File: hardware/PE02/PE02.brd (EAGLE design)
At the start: 25.4 x 25.4 mm, 24 parts, among them IC1 MSP430G2231, IC2 TPS78233

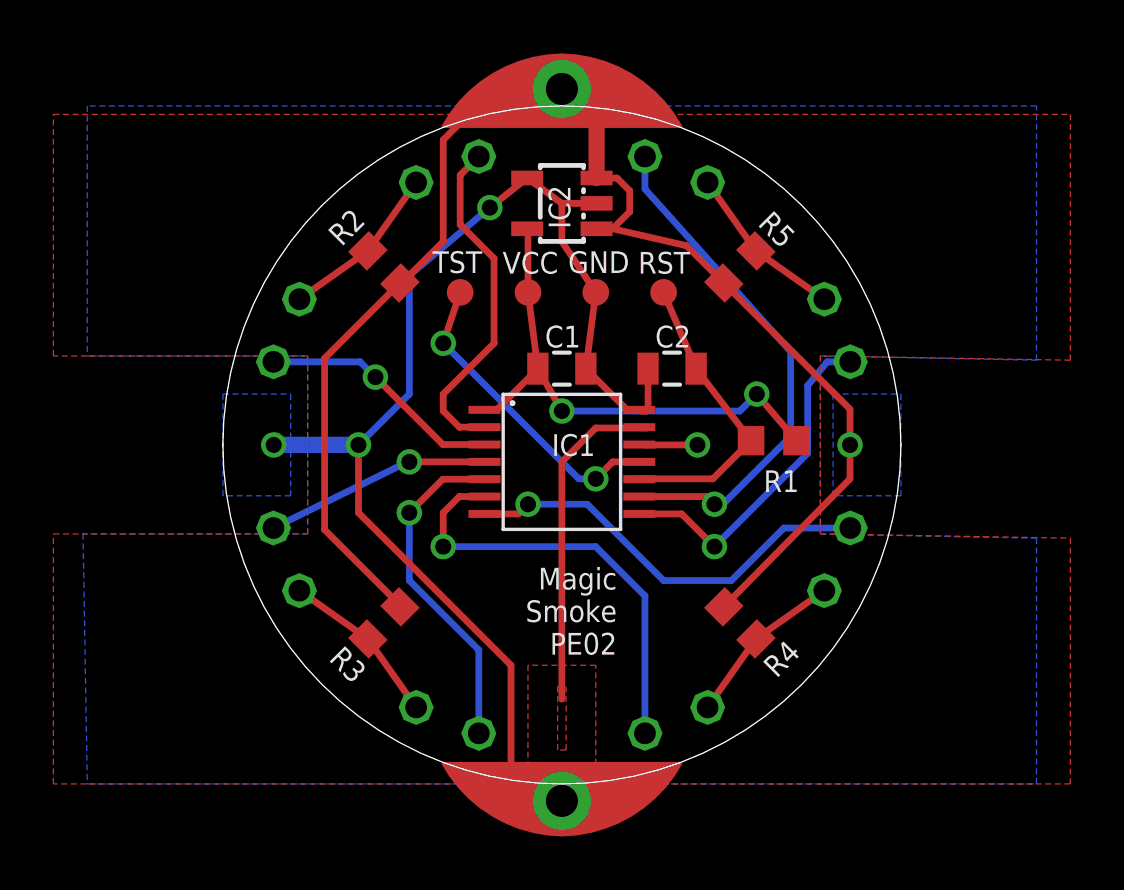
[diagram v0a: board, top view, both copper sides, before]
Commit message: Fixed buzzer, need to alter package of GND sewtab to make pad for vibration sensor
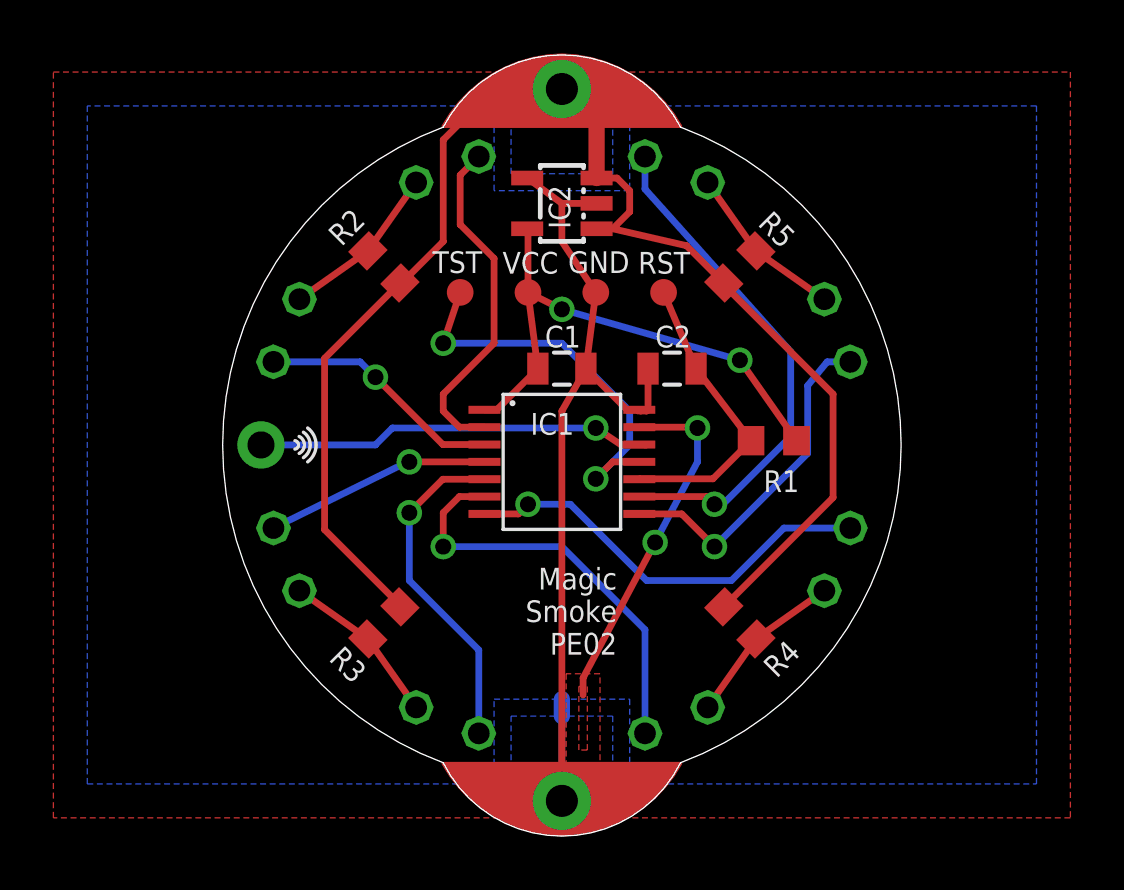
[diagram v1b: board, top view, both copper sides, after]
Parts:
- added JP1: (no value), adafruit:1X01-CLEANBIG
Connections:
- net BUZZ: now also JP1.1
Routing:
- net BUZZ: track 2.18 -> 15.2 mm
- net GND: track 47.0 -> 34.4 mm, vias 3 -> 0
- net TST: track 11.7 -> 15.0 mm
- net N$2: track 16.5 -> 15.8 mm
- net V+: track 54.2 -> 53.7 mm, vias 1 -> 0
- net VIB: track 12.9 -> 13.3 mm, vias 0 -> 2
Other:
- board size 25.4 x 25.4 mm -> 25.4 x 29.3 mm

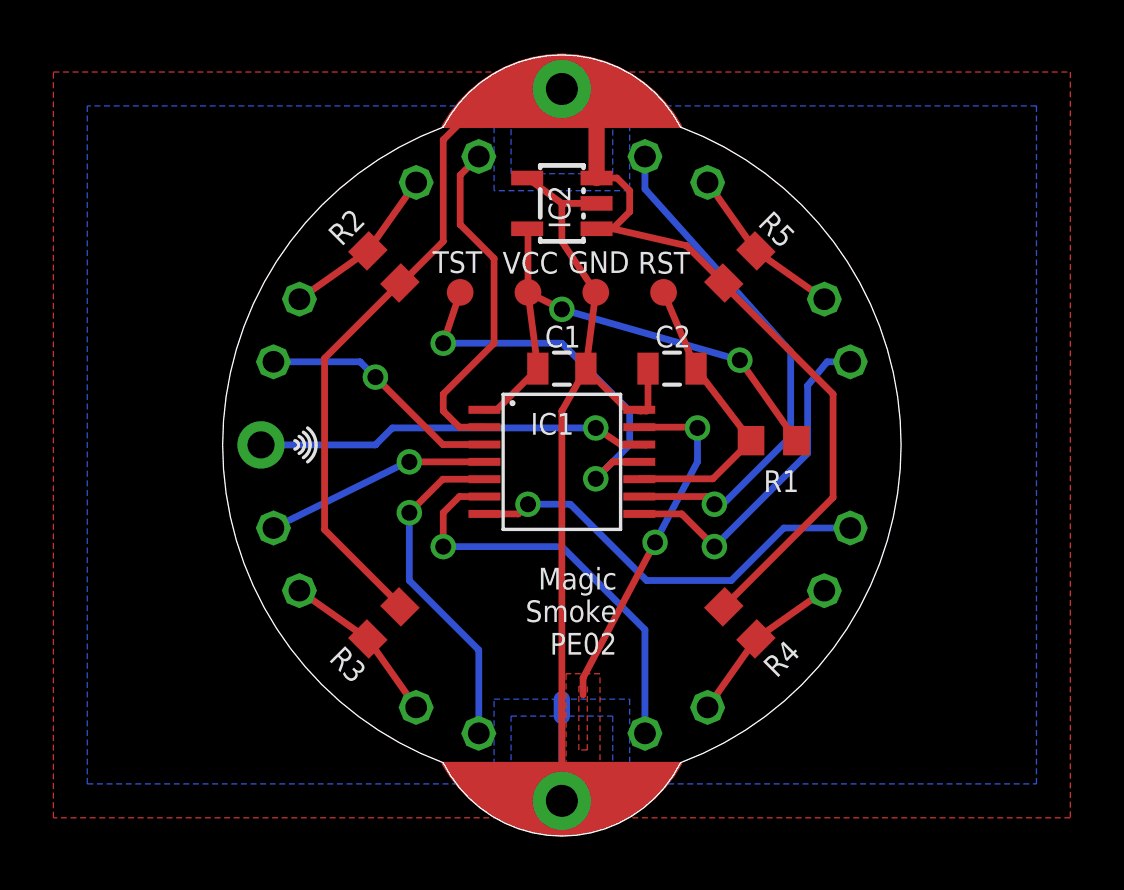
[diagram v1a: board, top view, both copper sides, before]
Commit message: 2.2V supply, pullup vibration sensor to output pin
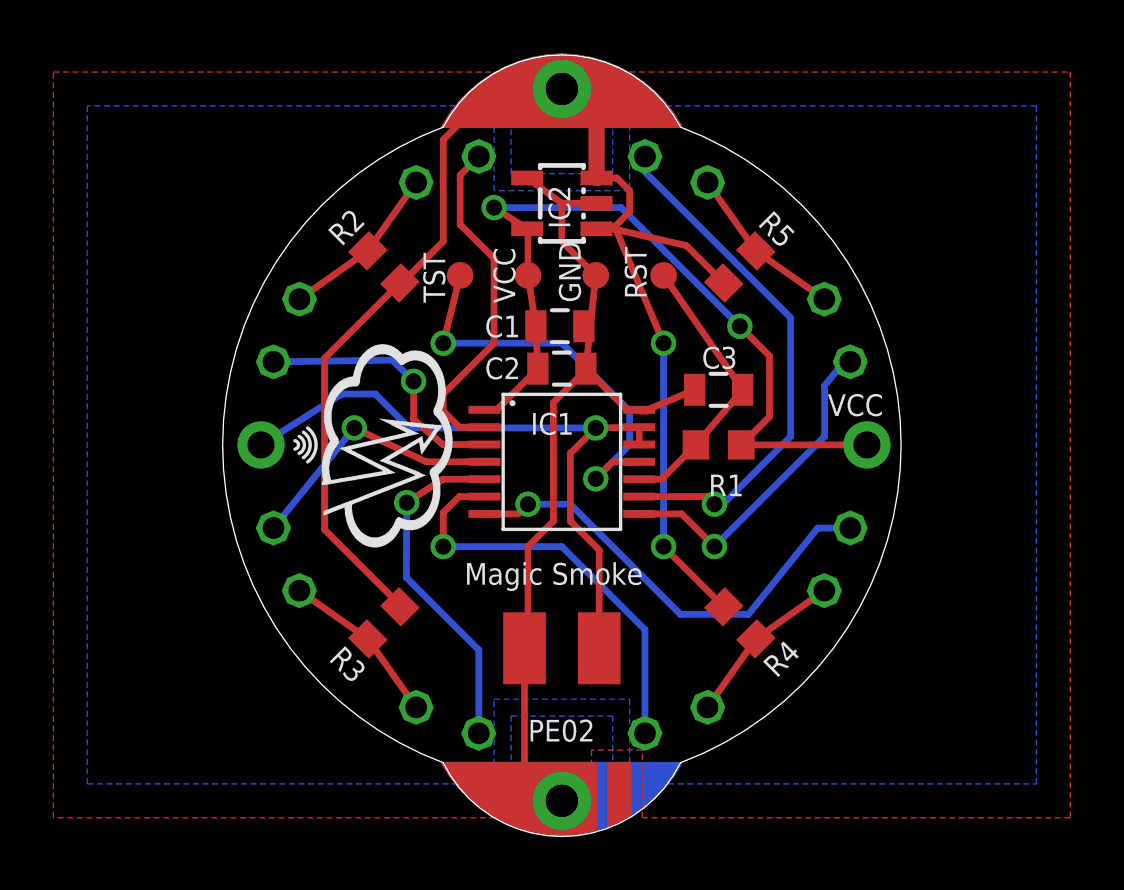
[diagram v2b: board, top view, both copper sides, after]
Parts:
- added C3: 1nF, SparkFun:0805
- added JP2: (no value), adafruit:1X01-CLEANBIG
- added MVS0608.02: (no value), rcl:R1210
- added TP3: SEWTAP0.4IN, adafruit:SEWINGTAP_0.4
- added TP4: SEWTAB, t0mpr1c3:SEWTAP_CUSTOM
- C1: value 100nF -> 1uF
- C2: value 1nF -> 100nF
- IC2: value TPS78233 -> TPS78222
- moved TP2 26.7 mm to (50.8, 69.2), flipped to the bottom, turned to 0 degrees
- moved C2 4.13 mm to (50.8, 58.7), turned to 0 degrees
- moved R1 2.07 mm to (56.7, 55.9)
- moved C1 1.59 mm to (50.7, 60.3)
- moved GND 0.63 mm to (52.1, 62.2)
- moved RST 0.63 mm to (54.6, 62.2)
- moved TST 0.63 mm to (47.0, 62.2)
- moved VCC 0.63 mm to (49.5, 62.2)
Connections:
- removed net +3V3: C1.1, IC1.1, IC2.5, R1.2, VCC.TP
- removed net BUZZ: IC1.12, JP1.1
- new net VCC: C1.1, C2.1, IC1.1, IC2.5, JP2.1, R1.2, VCC.TP
- net GND: now also C3.2, MVS0608.02.1, TP3.TAP, TP4.TAP; no longer TP2.TAP
- net RST: now also C3.1; no longer C2.1
- net V+: now also TP2.TAP
- net VIB: now also IC1.12, JP1.1, MVS0608.02.2
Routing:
- net VCC: track 0.00 -> 30.5 mm, vias 0 -> 2
- net +3V3: track 20.2 -> 0.00 mm, vias 2 -> 0
- net BUZZ: track 15.2 -> 0.00 mm, vias 1 -> 0
- net VIB: track 13.3 -> 25.3 mm, vias 2 -> 1
- net GND: track 34.4 -> 32.3 mm
- net N$6: track 8.65 -> 9.98 mm
- net N$1: track 15.9 -> 17.1 mm
- net N$7: track 9.19 -> 10.0 mm
- net RST: track 11.3 -> 10.6 mm
- net TST: track 15.0 -> 15.6 mm
- net V+: vias 0 -> 2
- removed copper zone on layer 1, net VIB
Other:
- board text added: "Magic Smoke"
- board text added: "PE02"
- board text added: "VCC"
- board text removed: "Magic Smoke PE02"

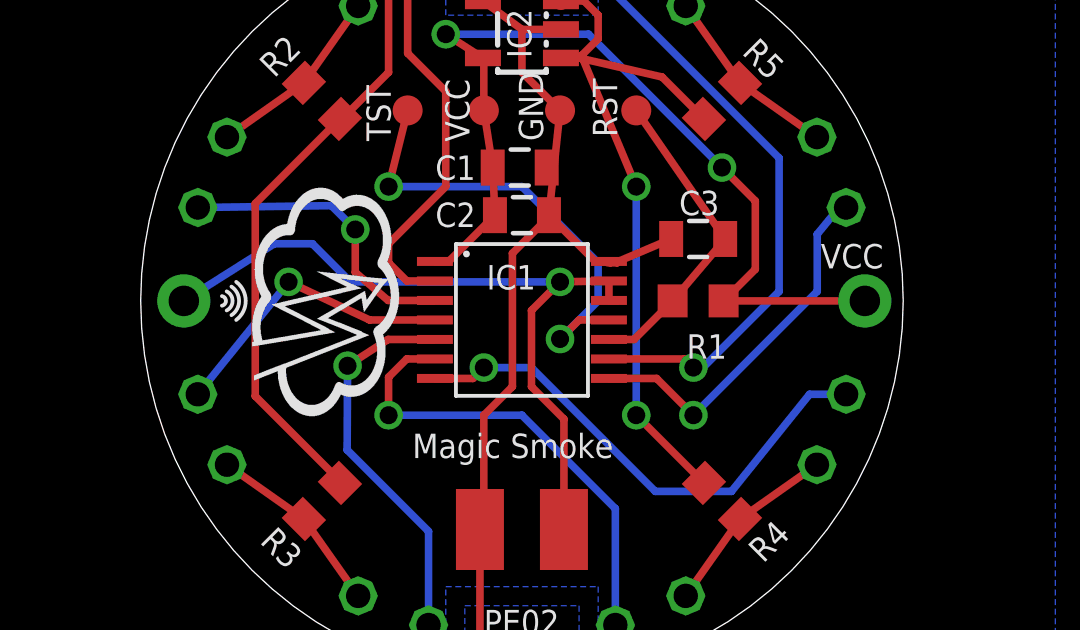
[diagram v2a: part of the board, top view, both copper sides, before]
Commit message: moved buzzer output to P1.2
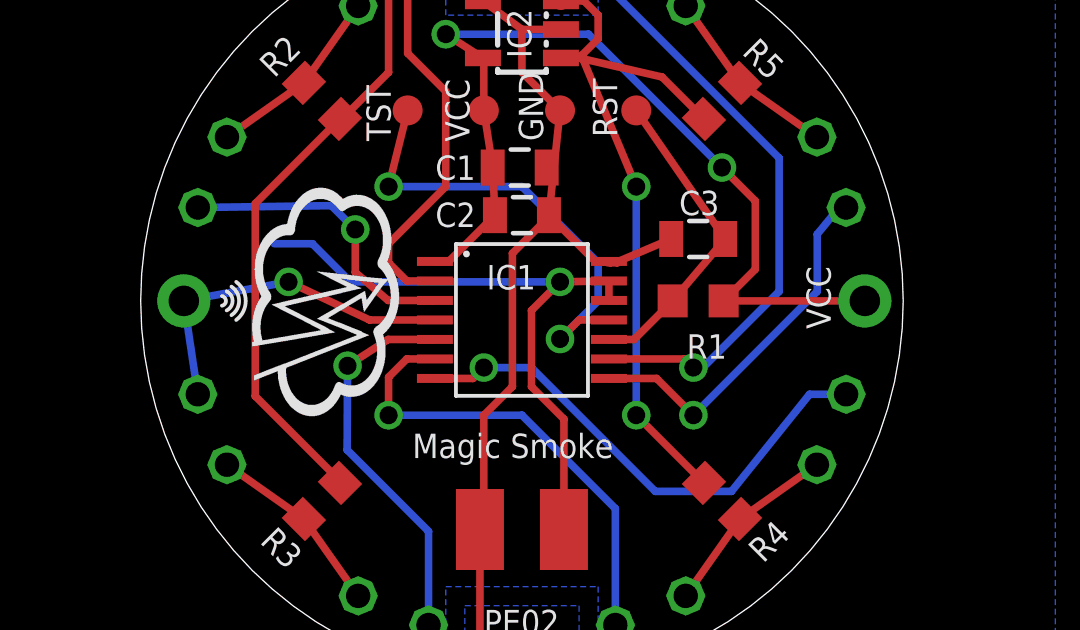
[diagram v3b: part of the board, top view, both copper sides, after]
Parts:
- JP1: value (none) -> BUZZER
- JP2: value (none) -> VCC
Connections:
- net N$6: now also JP1.1
- net VIB: no longer JP1.1
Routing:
- net VIB: track 25.3 -> 21.7 mm
- net N$6: track 9.98 -> 11.9 mm
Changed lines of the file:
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@@
 <wire x1="55.245" y1="67.78625" x2="55.245" y2="43.97375" width="0" layer="20" curve="-139.055441"/>
 <wire x1="46.355" y1="43.97375" x2="46.355" y2="67.78625" width="0" layer="20" curve="-139.055441"/>
-<text x="60.759584375" y="56.962790625" size="0.8128" layer="21" font="vector" ratio="15">VCC</text>
+<text x="61.095415625" y="54.94595625" size="0.8128" layer="21" font="vector" ratio="15" rot="R90">VCC</text>
 <text x="49.53" y="44.7675" size="0.8128" layer="21" font="vector" ratio="15">PE02</text>
 <rectangle x1="46.56155" y1="56.02903125" x2="46.84095" y2="56.04173125" layer="21" rot="R90"/>
@@
 <element name="TP1" library="adafruit" package="SEWINGTAP_0.4" value="SEWTAP0.4IN" x="50.8" y="69.215"/>
 <element name="TP2" library="adafruit" package="SEWINGTAP_0.4" value="SEWTAP0.4IN" x="50.8" y="69.215" rot="MR0"/>
-<element name="JP1" library="adafruit" package="1X01-CLEANBIG" value="" x="39.52875" y="55.88" smashed="yes">
-<attribute name="VALUE" x="38.25875" y="52.705" size="1.27" layer="27"/>
-</element>
+<element name="JP1" library="adafruit" package="1X01-CLEANBIG" value="BUZZER" x="39.52875" y="55.88" smashed="yes"/>
 <element name="TP3" library="adafruit" package="SEWINGTAP_0.4" value="SEWTAP0.4IN" x="50.8" y="42.545" rot="MR180"/>
 <element name="TP4" library="t0mpr1c3" package="SEWTAP_CUSTOM" value="SEWTAB" x="50.8" y="42.545" rot="R180"/>
-<element name="JP2" library="adafruit" package="1X01-CLEANBIG" value="" x="62.23" y="55.88" smashed="yes">
-<attribute name="VALUE" x="60.96" y="52.705" size="1.27" layer="27"/>
-</element>
+<element name="JP2" library="adafruit" package="1X01-CLEANBIG" value="VCC" x="62.23" y="55.88" smashed="yes"/>
 <element name="MVS0608.02" library="rcl" package="R1210" value="" x="50.8" y="48.26" smashed="yes">
 <attribute name="VALUE" x="48.26" y="45.085" size="1.27" layer="27"/>
@@
 <contactref element="MVS0608.02" pad="2"/>
 <contactref element="IC1" pad="12"/>
-<contactref element="JP1" pad="1"/>
 <via x="52.07" y="56.515" extent="1-16" drill="0.6" shape="square"/>
 <wire x1="53.975" y1="55.88" x2="53.7" y2="55.895" width="0.254" layer="1"/>
@@
 <wire x1="45.085" y1="56.515" x2="43.815" y2="57.785" width="0.254" layer="16"/>
 <wire x1="43.815" y1="57.785" x2="42.545" y2="57.785" width="0.254" layer="16"/>
-<wire x1="42.545" y1="57.785" x2="39.52875" y2="55.88" width="0.254" layer="16"/>
 </signal>
 <signal name="VCC">
@@
 <wire x1="45.72" y1="55.245" x2="43.02125" y2="56.515" width="0.254" layer="1"/>
 <via x="43.02125" y="56.515" extent="1-16" drill="0.6" shape="square"/>
-<wire x1="43.02125" y1="56.515" x2="39.99524375" y2="52.767075" width="0.254" layer="16"/>
-</signal>
-<signal name="N$7">
-<contactref element="IC1" pad="3"/>
-<contactref element="D2" pad="K"/>
-<wire x1="47.8999" y1="55.895" x2="46.34" y2="55.895" width="0.254" layer="1"/>
-<wire x1="46.34" y1="55.895" x2="45.24375" y2="56.8325" width="0.254" layer="1"/>
-<wire x1="45.24375" y1="56.8325" x2="45.24375" y2="58.26125" width="0.254" layer="1"/>
-<via x="45.24375" y="58.26125" extent="1-16" drill="0.6" shape="square"/>
-<wire x1="45.24375" y1="58.26125" x2="44.45" y2="59.055" width="0.254" layer="16"/>
-<wire x1="44.45" y1="59.055" x2="39.99524375" y2="58.992921875" width="0.254" layer="16"/>
+<contactref element="JP1" pad="1"/>
+<wire x1="39.52875" y1="55.88" x2="39.99524375" y2="52.767075" width="0.254" layer="16"/>
+<wire x1="39.52875" y1="55.88" x2="43.02125" y2="56.515" width="0.254" layer="16"/>
 </signal>
 <signal name="N$8">
@@
 <wire x1="54.61" y1="52.07" x2="54.61" y2="59.69" width="0.254" layer="16"/>
 </signal>
+<signal name="N$12">
+<contactref element="IC1" pad="3"/>
+<contactref element="D2" pad="K"/>
+<wire x1="47.8999" y1="55.895" x2="46.34" y2="55.895" width="0.254" layer="1"/>
+<wire x1="46.34" y1="55.895" x2="45.24375" y2="56.8325" width="0.254" layer="1"/>
+<wire x1="45.24375" y1="56.8325" x2="45.24375" y2="58.26125" width="0.254" layer="1"/>
+<via x="45.24375" y="58.26125" extent="1-16" drill="0.6" shape="square"/>
+<wire x1="45.24375" y1="58.26125" x2="44.45" y2="59.055" width="0.254" layer="16"/>
+<wire x1="44.45" y1="59.055" x2="39.99524375" y2="58.992921875" width="0.254" layer="16"/>
+</signal>
 </signals>

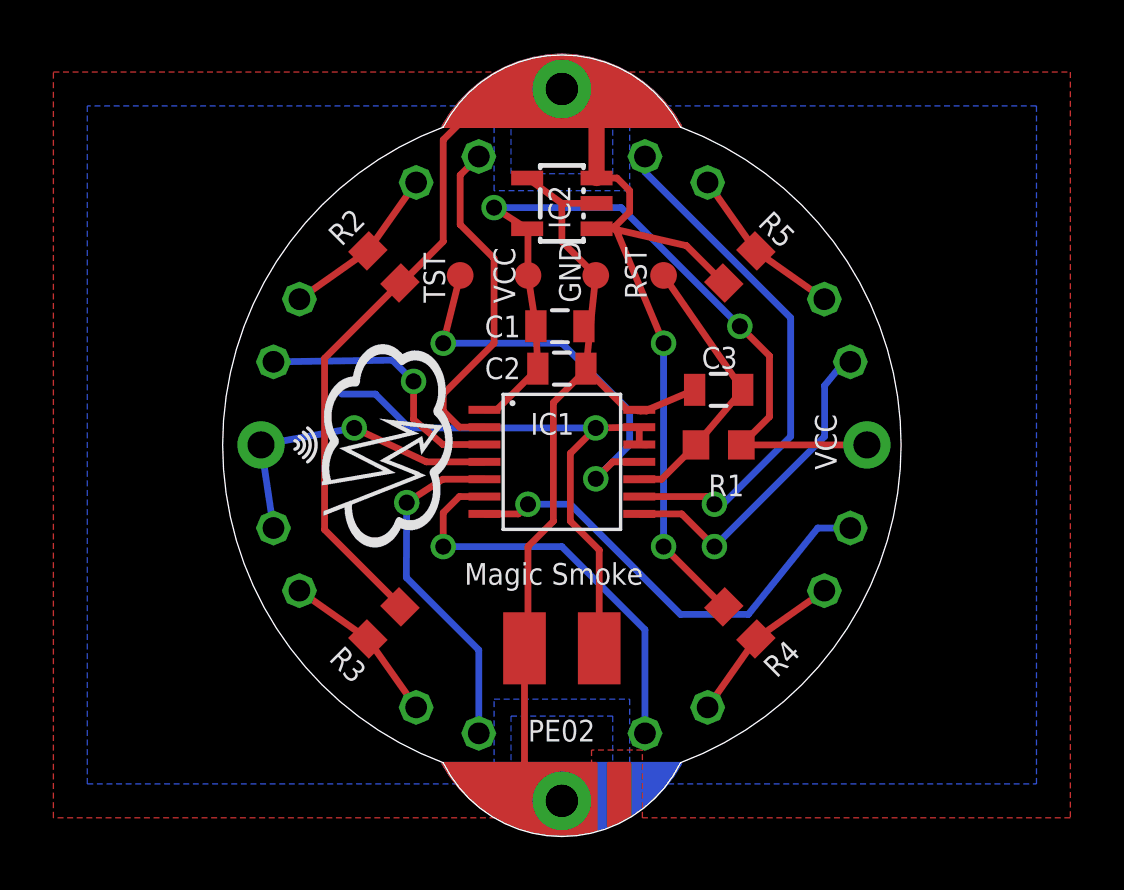
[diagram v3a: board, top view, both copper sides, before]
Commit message: Added Molex Pico-EZmate connector, removed bottom sewtab
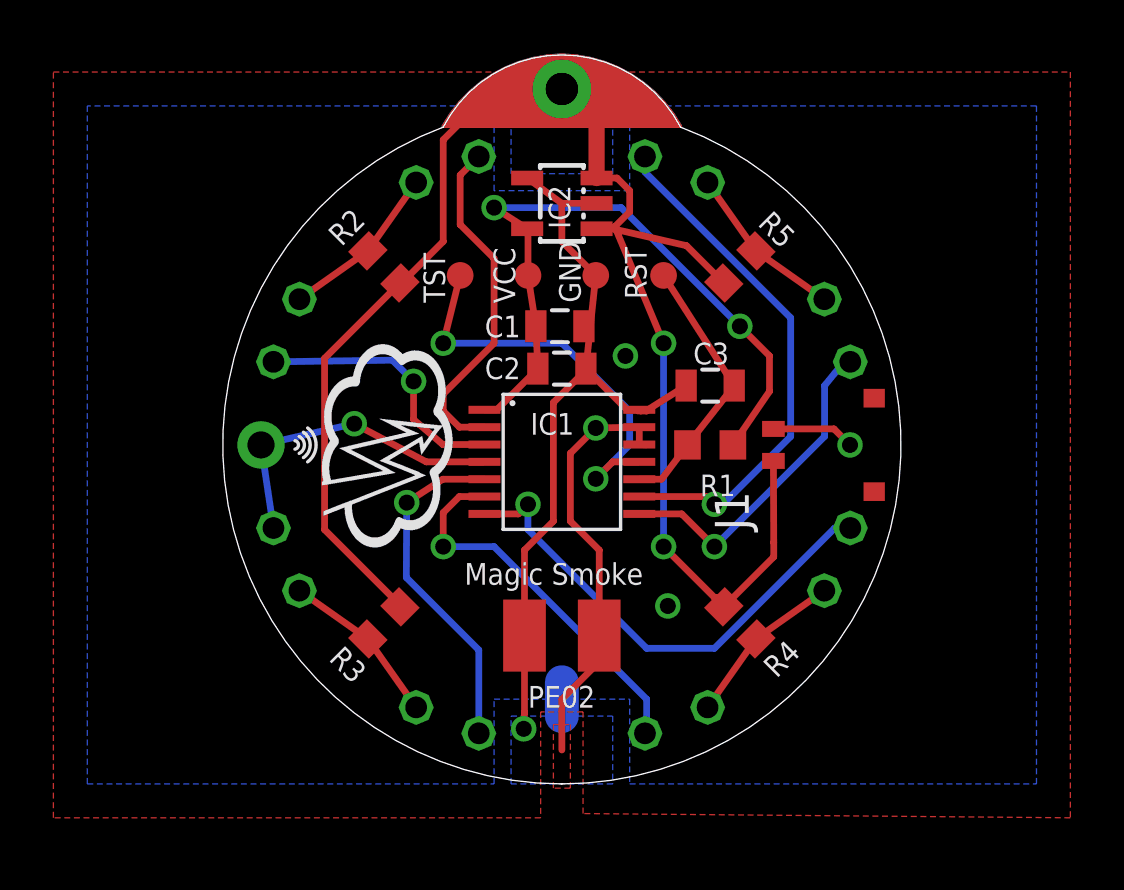
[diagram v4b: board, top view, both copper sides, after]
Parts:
- removed JP2: VCC, adafruit:1X01-CLEANBIG
- removed TP3: SEWTAP0.4IN, adafruit:SEWINGTAP_0.4
- removed TP4: SEWTAB, t0mpr1c3:SEWTAP_CUSTOM
- added J1: 78171-0002, con-molex-pico-ezmate:78171-0002
- MVS0608.02: value (none) -> VIBRATION SENSOR
- R2, R3, R4, R5: value 100 -> 56
- moved MVS0608.02 0.48 mm to (50.8, 48.7)
- moved C3 0.35 mm to (56.4, 58.1)
- moved R1 0.32 mm to (56.4, 55.9)
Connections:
- net GND: now also J1.2; no longer TP3.TAP, TP4.TAP
- net V+: now also J1.1
- net VCC: no longer JP2.1
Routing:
- net V+: track 53.7 -> 60.6 mm
- net VCC: track 30.5 -> 25.8 mm
- net VIB: track 21.7 -> 17.3 mm
- net N$2: track 15.8 -> 14.4 mm
- net N$1: track 17.1 -> 18.5 mm
- net GND: track 32.3 -> 33.2 mm, vias 0 -> 4
- added copper zone on layer 1, net VIB
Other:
- board size 25.4 x 29.3 mm -> 25.4 x 27.3 mm
- board text removed: "VCC"
